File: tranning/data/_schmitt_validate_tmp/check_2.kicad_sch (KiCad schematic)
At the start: 3 parts, among them U1 LM358

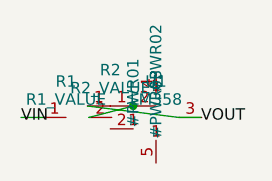
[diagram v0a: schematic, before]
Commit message: Fix overlapping and mis-wired schematics; add ESP32, Mega 2560, Pi 5
- circuit_rule_check.transform_point: flip the library y axis. Verified
  against KiCad's own demo schematics (42/42 and 182/182 pins on a wire);
  the old formula made generated files open in KiCad with +5V on the GND
  pin and the reset pull-up on PB0.
- circuit_ic_generator: rewritten layout. IC pins get a short stub to an
  outward-facing power symbol or a net label; decoupling, reset and
  crystal circuits are measured blocks stacked beside the IC, checked for
  overlap before writing; drawing placed on an auto-sized page; library
  symbols get graphics. Adds ESP32-WROOM-32, ATmega2560, Pi 5 header.
- circuit_rule_check: same-name nets are joined (KiCad behaviour), new
  overlapping_symbols rule, 3V3/EN pin names recognised.
- circuit_kicad_to_schemdraw: draws labels, power flags and IC pin names;
  pin side taken from the pin's own direction.
- schmitt_trigger_gen: library block fixed so KiCad wires IN+/IN- and
  V+/V- as intended and power pins join GND/VCC; model output unchanged.
- Tests: 65 pass, including a real kicad-cli netlist check.

Co-Authored-By: Claude Opus 5.5 <noreply@anthropic.com>
Claude-Session: https://claude.ai/code/session_01TWSKnHncRvWd1K9A45SkP5
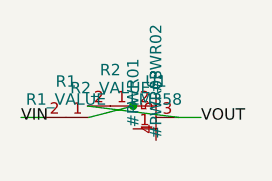
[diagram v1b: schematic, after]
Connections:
- net VIN: now also R1.2; no longer R1.1
- net VOUT: now also R2.2; no longer R2.1
- net at U1.2: now also R1.1, R2.1
- net VCC: now reaches U1.4
- net GND: now reaches U1.5
- net GND: now also U1.1
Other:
- moved on the sheet: R1, R2, U1

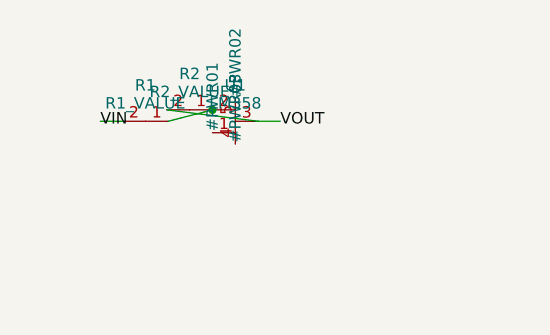
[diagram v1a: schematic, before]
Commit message: Redesign Schmitt-trigger templates without overlaps (retrain in progress)
- schmitt_trigger_gen: KiCad-sized op-amp/resistor/inverter symbols with
  graphics; every pin position computed with transform_point; orthogonal
  wiring with the feedback resistor routed above/below the op-amp; labels
  and power-net names placed away from parts; power references hidden.
  uuids are added by wrap_kicad() instead of the model (~90 tokens less
  per circuit), so the longest pair is 990 tokens (block_size 1024).
  validate_pairs now rejects overlap warnings too.
- circuit_rule_check: a multi-pin part's body is where its pins end (tip
  plus pin length), so supply symbols on an op-amp's V+/V- tips are not
  counted as overlapping it.
- schmitt_trigger_train: --checkpoint-every (default 10) for long runs.
- Tests: real-KiCad netlist check for four topologies; context-length check.

The checked-in schmitt model still matches the old templates until the
retrain running now finishes.

Co-Authored-By: Claude Opus 5.5 <noreply@anthropic.com>
Claude-Session: https://claude.ai/code/session_01TWSKnHncRvWd1K9A45SkP5
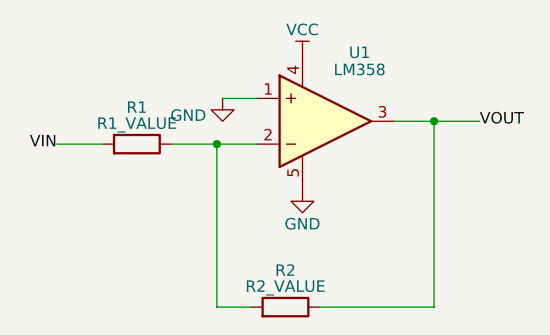
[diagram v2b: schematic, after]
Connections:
- net VIN: now also R1.1; no longer R1.2
- net at R2.1, U1.2: now also R1.2; no longer R1.1
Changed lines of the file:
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@@
 (kicad_sch (version 20231120) (generator sinco_schmitt_gen) (paper "A4")
- (symbol (lib_id "Sinco:R") (at 100.0 100.0 0) (unit 1)(property "Reference" "R1" (at 100.0 96.0 0)) (property "Value" "R1_VALUE" (at 100.0 98.0 0)))(symbol (lib_id "Sinco:R") (at 104.91999999999999 98.73 0) (unit 1)(property "Reference" "R2" (at 104.91999999999999 94.73 0)) (property "Value" "R2_VALUE" (at 104.91999999999999 96.73 0)))(symbol (lib_id "Sinco:OpAmp") (at 110.0 100.0 0) (unit 1)(property "Reference" "U1" (at 110.0 96.0 0)) (property "Value" "LM358" (at 110.0 98.0 0)))(symbol (lib_id "power:GND") (at 107.46 101.27 90) (unit 1)(property "Reference" "#PWR01" (at 107.46 97.27 0)) )(symbol (lib_id "power:GND") (at 110.0 97.46 90) (unit 1)(property "Reference" "#PWR02" (at 110.0 93.46 0)) )(symbol (lib_id "power:VCC") (at 110.0 102.54 90) (unit 1)(property "Reference" "#PWR03" (at 110.0 98.54 0)) )(wire (pts (xy 95.0 100.0) (xy 97.46 100.0)))(wire (pts (xy 102.54 100.0) (xy 107.46 98.73)))(wire (pts (xy 102.37999999999998 98.73) (xy 112.54 100.0)))(wire (pts (xy 112.54 100.0) (xy 115.0 100.0)))(junction (at 107.46 98.73))(label "VIN" (at 95.0 100.0 0))(label "VOUT" (at 115.0 100.0 0)))
+ (symbol (lib_id "Sinco:R") (at 99.06 102.54 0) (unit 1) (property "Reference" "R1" (at 99.06 98.476 0)) (property "Value" "R1_VALUE" (at 99.06 100.254 0)))(symbol (lib_id "Sinco:R") (at 115.57 120.65 0) (unit 1) (property "Reference" "R2" (at 115.57 116.58600000000001 0)) (property "Value" "R2_VALUE" (at 115.57 118.364 0)))(wire (pts (xy 107.95 102.54) (xy 107.95 120.65)))(wire (pts (xy 107.95 120.65) (xy 111.76 120.65)))(wire (pts (xy 119.38 120.65) (xy 132.08 120.65)))(wire (pts (xy 132.08 120.65) (xy 132.08 100.0)))(junction (at 132.08 100.0))(symbol (lib_id "Sinco:OpAmp") (at 120.0 100.0 0) (unit 1) (property "Reference" "U1" (at 123.81 92.38 0)) (property "Value" "LM358" (at 123.81 94.285 0)))(symbol (lib_id "power:VCC") (at 117.46 92.38 0) (unit 1) (property "Reference" "#PWR01" (at 117.46 88.316 0) (effects hide)) (property "Value" "VCC" (at 117.46 89.83999999999999 0)))(symbol (lib_id "power:GND") (at 117.46 107.62 0) (unit 1) (property "Reference" "#PWR02" (at 117.46 103.55600000000001 0) (effects hide)) (property "Value" "GND" (at 117.46 111.43 0)))(wire (pts (xy 127.62 100.0) (xy 132.08 100.0)))(wire (pts (xy 132.08 100.0) (xy 137.16 100.0)))(symbol (lib_id "power:GND") (at 108.585 97.46 0) (unit 1) (property "Reference" "#PWR03" (at 108.585 93.39599999999999 0) (effects hide)) (property "Value" "GND" (at 104.77499999999999 99.365 0)))(wire (pts (xy 90.17 102.54) (xy 95.25 102.54)))(wire (pts (xy 102.87 102.54) (xy 107.95 102.54)))(wire (pts (xy 107.95 102.54) (xy 112.38 102.54)))(wire (pts (xy 112.38 97.46) (xy 108.585 97.46)))(junction (at 107.95 102.54))(label "VIN" (at 90.17 102.54 180))(label "VOUT" (at 137.16 100.0 0)))
